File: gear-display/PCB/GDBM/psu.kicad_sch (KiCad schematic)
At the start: 11 parts, among them J3 DC_2.5_5.5_PJ-090BH, U1 DC_DC_5V_2A0_GAPTEC_OKI-78SR-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

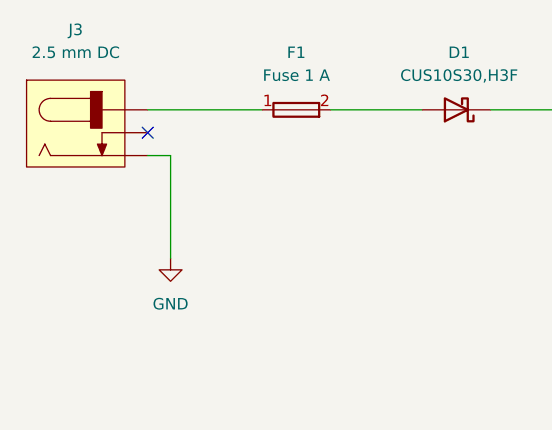
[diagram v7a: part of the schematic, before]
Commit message: bugfixes
added 555 circuit for brightness control
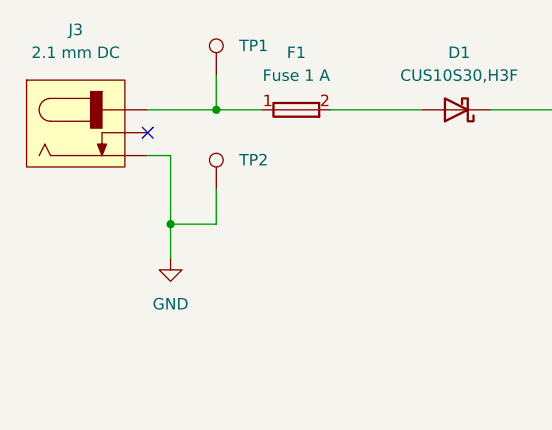
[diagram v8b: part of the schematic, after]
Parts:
- added TP1, TP2: TestPoint_2.5mm_Round, KD_Connector_Pads:TestPoint_Pad_D2.5mm, symbol KD_Connector_Pads:TestPoint_2.5mm_Round
- J3: value DC_2.5_5.5_PJ-090BH -> DC_2.1_5.5_54-00286; footprint KD_Connector_Circular:CON_DC_2.5_5.5_PJ-090BH -> KD_Connector_Circular:CON_DC_2.1_5.5_Tensility_54-00286; symbol KD_Connector_Circular:DC_2.5_5.5_PJ-090BH -> KD_Connector_Circular:DC_2.1_5.5_54-00286; Code 2.5 mm DC -> 2.1 mm DC; MFG_PartNo PJ-090BH -> 54-00286; Price 1.7 -> 0.7; Supplier_PartNo 102-5562-1-ND -> 839-54-00286-ND
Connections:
- net Earth: now also J3.B (SLEEVE), TP2.1; no longer J3.2 (SLEEVE), J3.4 (CENTER)
- net at F1.1: now also J3.A (CENTER), TP1.1; no longer J3.1 (CENTER)
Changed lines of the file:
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@@
   (junction (at 181.61 97.79) (diameter 0) (color 0 0 0 0)
   )
+  (junction (at 107.95 48.26) (diameter 0) (color 0 0 0 0)
+  )
   (junction (at 195.58 97.79) (diameter 0) (color 0 0 0 0)
   )
+  (junction (at 102.87 60.96) (diameter 0) (color 0 0 0 0)
+  )
   (junction (at 195.58 48.26) (diameter 0) (color 0 0 0 0)
   )
@@
   )
   (no_connect (at 100.33 50.8))
+  (wire (pts (xy 102.87 60.96) (xy 102.87 64.77))
+    (stroke (width 0) (type default) (color 0 0 0 0))
+  )
   (wire (pts (xy 160.02 48.26) (xy 177.8 48.26))
     (stroke (width 0) (type default) (color 0 0 0 0))
@@
     (stroke (width 0) (type default) (color 0 0 0 0))
   )
+  (wire (pts (xy 102.87 60.96) (xy 107.95 60.96))
+    (stroke (width 0) (type default) (color 0 0 0 0))
+  )
   (wire (pts (xy 167.64 97.79) (xy 181.61 97.79))
     (stroke (width 0) (type default) (color 0 0 0 0))
@@
     (stroke (width 0) (type default) (color 0 0 0 0))
   )
-  (wire (pts (xy 100.33 48.26) (xy 113.03 48.26))
+  (wire (pts (xy 107.95 48.26) (xy 113.03 48.26))
+    (stroke (width 0) (type default) (color 0 0 0 0))
+  )
+  (wire (pts (xy 100.33 48.26) (xy 107.95 48.26))
     (stroke (width 0) (type default) (color 0 0 0 0))
   )
@@
     (stroke (width 0) (type default) (color 0 0 0 0))
   )
-  (wire (pts (xy 102.87 53.34) (xy 102.87 64.77))
+  (wire (pts (xy 102.87 53.34) (xy 102.87 60.96))
+    (stroke (width 0) (type default) (color 0 0 0 0))
+  )
+  (wire (pts (xy 107.95 44.45) (xy 107.95 48.26))
     (stroke (width 0) (type default) (color 0 0 0 0))
   )
@@
   )
   (wire (pts (xy 160.02 58.42) (xy 160.02 64.77))
+    (stroke (width 0) (type default) (color 0 0 0 0))
+  )
+  (wire (pts (xy 107.95 57.15) (xy 107.95 60.96))
     (stroke (width 0) (type default) (color 0 0 0 0))
   )
@@
     (pin "1")
   )
+  (symbol (lib_id "KD_Connector_Pads:TestPoint_2.5mm_Round") (at 107.95 44.45 0) (unit 1)
+    (in_bom yes) (on_board yes) (fields_autoplaced)
+    (property "Reference" "TP1" (id 0) (at 110.49 41.1479 0)
+      (effects (font (size 1.27 1.27)) (justify left))
+    )
+    (property "Value" "TestPoint_2.5mm_Round" (id 1) (at 95.25 12.7 0)
+      (effects (font (size 1.27 1.27)) (justify left) hide)
+    )
+    (property "Footprint" "KD_Connector_Pads:TestPoint_Pad_D2.5mm" (id 2) (at 95.25 30.48 0)
+      (effects (font (size 1.27 1.27)) (justify left) hide)
+    )
+    (property "Datasheet" "DNP" (id 3) (at 95.25 33.02 0)
+      (effects (font (size 1.27 1.27)) (justify left) hide)
+    )
+    (property "Code" "DNP" (id 4) (at 95.25 35.56 0)
+      (effects (font (size 1.27 1.27)) (justify left) hide)
+    )
+    (property "Manufacturer" "DNP" (id 5) (at 95.25 15.24 0)
+      (effects (font (size 1.27 1.27)) (justify left) hide)
+    )
+    (property "MFG_PartNo" "DNP" (id 6) (at 95.25 17.78 0)
+      (effects (font (size 1.27 1.27)) (justify left) hide)
+    )
+    (property "Supplier" "DNP" (id 7) (at 95.25 20.32 0)
+      (effects (font (size 1.27 1.27)) (justify left) hide)
+    )
+    (property "Supplier_PartNo" "DNP" (id 8) (at 95.25 22.86 0)
+      (effects (font (size 1.27 1.27)) (justify left) hide)
+    )
+    (property "DNP" "T" (id 9) (at 95.25 25.4 0)
+      (effects (font (size 1.27 1.27)) (justify left) hide)
+    )
+    (property "Price" "0.00" (id 10) (at 95.25 27.94 0)
+      (effects (font (size 1.27 1.27)) (justify left) hide)
+    )
+    (pin "1")
+  )
   (symbol (lib_id "KD_Capacitor:C_0603_100n_X7R_100V") (at 195.58 105.41 0) (unit 1)
     (in_bom yes) (on_board yes) (fields_autoplaced)
@@
     (pin "1")
   )
-  (symbol (lib_id "KD_Connector_Circular:DC_2.5_5.5_PJ-090BH") (at 100.33 48.26 0) (unit 1)
+  (symbol (lib_id "KD_Connector_Circular:DC_2.1_5.5_54-00286") (at 100.33 48.26 0) (unit 1)
     (in_bom yes) (on_board yes) (fields_autoplaced)
     (property "Reference" "J3" (id 0) (at 92.329 39.37 0))
-    (property "Value" "DC_2.5_5.5_PJ-090BH" (id 1) (at 87.63 16.51 0)
-      (effects (font (size 1.27 1.27)) (justify left) hide)
-    )
-    (property "Footprint" "KD_Connector_Circular:CON_DC_2.5_5.5_PJ-090BH" (id 2) (at 87.63 34.29 0)
-      (effects (font (size 1.27 1.27)) (justify left) hide)
-    )
-    (property "Datasheet" "https://www.cuidevices.com/product/resource/digikeypdf/pj-102b.pdf" (id 3) (at 87.63 36.83 0)
-      (effects (font (size 1.27 1.27)) (justify left) hide)
-    )
-    (property "Code" "2.5 mm DC" (id 4) (at 92.329 41.91 0))
+    (property "Value" "DC_2.1_5.5_54-00286" (id 1) (at 87.63 16.51 0)
+      (effects (font (size 1.27 1.27)) (justify left) hide)
+    )
+    (property "Footprint" "KD_Connector_Circular:CON_DC_2.1_5.5_Tensility_54-00286" (id 2) (at 87.63 34.29 0)
+      (effects (font (size 1.27 1.27)) (justify left) hide)
+    )
+    (property "Datasheet" "http://www.tensility.com/pdffiles/54-00286.pdf" (id 3) (at 87.63 36.83 0)
+      (effects (font (size 1.27 1.27)) (justify left) hide)
+    )
+    (property "Code" "2.1 mm DC" (id 4) (at 92.329 41.91 0))
     (property "Manufacturer" "CUI Devices" (id 5) (at 87.63 19.05 0)
       (effects (font (size 1.27 1.27)) (justify left) hide)
     )
-    (property "MFG_PartNo" "PJ-090BH" (id 6) (at 87.63 21.59 0)
+    (property "MFG_PartNo" "54-00286" (id 6) (at 87.63 21.59 0)
       (effects (font (size 1.27 1.27)) (justify left) hide)
     )
@@
       (effects (font (size 1.27 1.27)) (justify left) hide)
     )
-    (property "Supplier_PartNo" "102-5562-1-ND" (id 8) (at 87.63 26.67 0)
+    (property "Supplier_PartNo" "839-54-00286-ND" (id 8) (at 87.63 26.67 0)
       (effects (font (size 1.27 1.27)) (justify left) hide)
     )
@@
       (effects (font (size 1.27 1.27)) (justify left) hide)
     )
-    (property "Price" "1.7" (id 10) (at 87.63 31.75 0)
-      (effects (font (size 1.27 1.27)) (justify left) hide)
-    )
-    (pin "1")
-    (pin "2")
-    (pin "3")
-    (pin "4")
+    (property "Price" "0.7" (id 10) (at 87.63 31.75 0)
+      (effects (font (size 1.27 1.27)) (justify left) hide)
+    )
+    (pin "A")
+    (pin "B")
+    (pin "C")
+  )
+  (symbol (lib_id "KD_Connector_Pads:TestPoint_2.5mm_Round") (at 107.95 57.15 0) (unit 1)
+    (in_bom yes) (on_board yes) (fields_autoplaced)
+    (property "Reference" "TP2" (id 0) (at 110.49 53.8479 0)
+      (effects (font (size 1.27 1.27)) (justify left))
+    )
+    (property "Value" "TestPoint_2.5mm_Round" (id 1) (at 95.25 25.4 0)
+      (effects (font (size 1.27 1.27)) (justify left) hide)
+    )
+    (property "Footprint" "KD_Connector_Pads:TestPoint_Pad_D2.5mm" (id 2) (at 95.25 43.18 0)
+      (effects (font (size 1.27 1.27)) (justify left) hide)
+    )
+    (property "Datasheet" "DNP" (id 3) (at 95.25 45.72 0)
+      (effects (font (size 1.27 1.27)) (justify left) hide)
+    )
+    (property "Code" "DNP" (id 4) (at 95.25 48.26 0)
+      (effects (font (size 1.27 1.27)) (justify left) hide)
+    )
+    (property "Manufacturer" "DNP" (id 5) (at 95.25 27.94 0)
+      (effects (font (size 1.27 1.27)) (justify left) hide)
+    )
+    (property "MFG_PartNo" "DNP" (id 6) (at 95.25 30.48 0)
+      (effects (font (size 1.27 1.27)) (justify left) hide)
+    )
+    (property "Supplier" "DNP" (id 7) (at 95.25 33.02 0)
+      (effects (font (size 1.27 1.27)) (justify left) hide)
+    )
+    (property "Supplier_PartNo" "DNP" (id 8) (at 95.25 35.56 0)
+      (effects (font (size 1.27 1.27)) (justify left) hide)
+    )
+    (property "DNP" "T" (id 9) (at 95.25 38.1 0)
+      (effects (font (size 1.27 1.27)) (justify left) hide)
+    )
+    (property "Price" "0.00" (id 10) (at 95.25 40.64 0)
+      (effects (font (size 1.27 1.27)) (justify left) hide)
+    )
+    (pin "1")
   )
   (symbol (lib_id "KD_Capacitor:C_0805_22u_X5R_10V") (at 128.27 104.14 0) (unit 1)
